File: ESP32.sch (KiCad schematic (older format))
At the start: 31 parts, among them J201 Conn_02x13_Odd_Even, J202 Conn_02x10_Odd_Even, J203 Conn_01x02, J204 Conn_01x06, J206 IO, J207 Conn_01x07, U201 ESP32-WROOM-32D

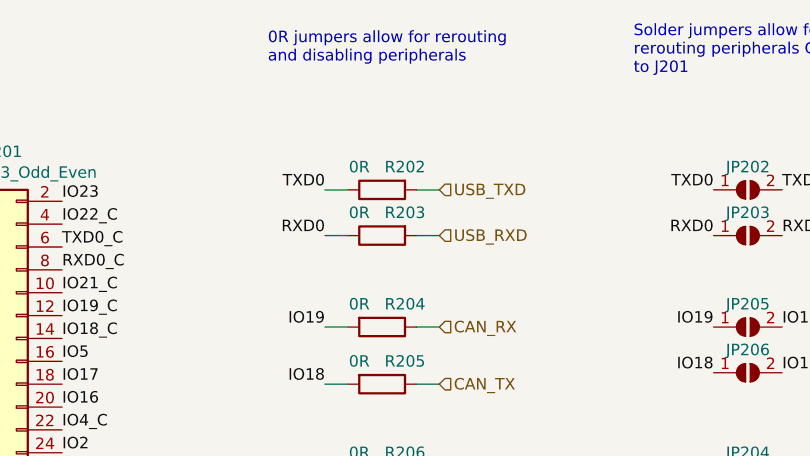
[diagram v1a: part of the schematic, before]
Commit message: - Swapped TXD0 & RXD0 between ESP32 and CH340C (U401) - (at the 0 Ohm Links) - U401 -> Pin 16 (VCC switched to 3V3) - U401 ->  Pin 4 (V3)  taken to 3V3
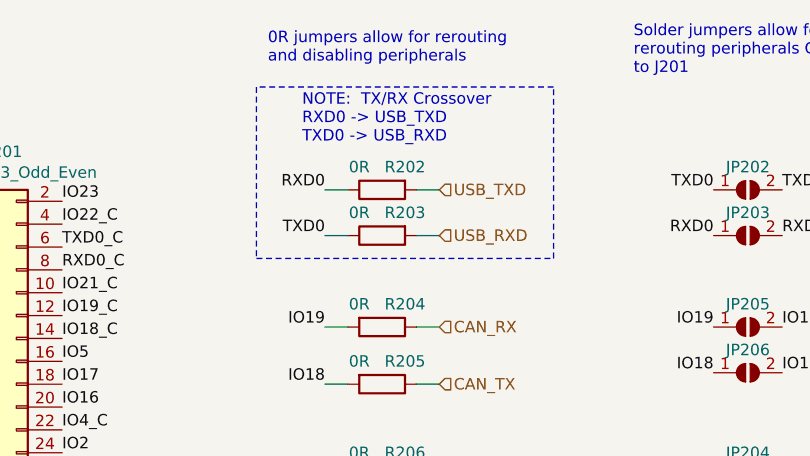
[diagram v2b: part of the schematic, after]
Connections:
- net RXD0: now also R202.1; no longer R203.1
- net TXD0: now also R203.1; no longer R202.1
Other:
- note added: "NOTE: TX/RX Crossover\nRXD0 -> USB_TXD \nTXD0 -> USB_RXD"
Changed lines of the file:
@@
 	0    -1   1    0
 $EndComp
+Text Label 7350 1650 2    50   ~ 0
+TXD0
 Text Label 7350 1450 2    50   ~ 0
-TXD0
-Text Label 7350 1650 2    50   ~ 0
 RXD0
 Wire Wire Line
@@
 Wire Wire Line
 	3750 7100 4150 7100
+Text Notes 7250 1250 0    50   ~ 0
+NOTE:  TX/RX Crossover\nRXD0 -> USB_TXD  \nTXD0 -> USB_RXD
+Wire Notes Line
+	7050 1750 8350 1750
+Wire Notes Line
+	8350 1750 8350 1000
+Wire Notes Line
+	8350 1000 7050 1000
+Wire Notes Line
+	7050 1000 7050 1750
 $EndSCHEMATC

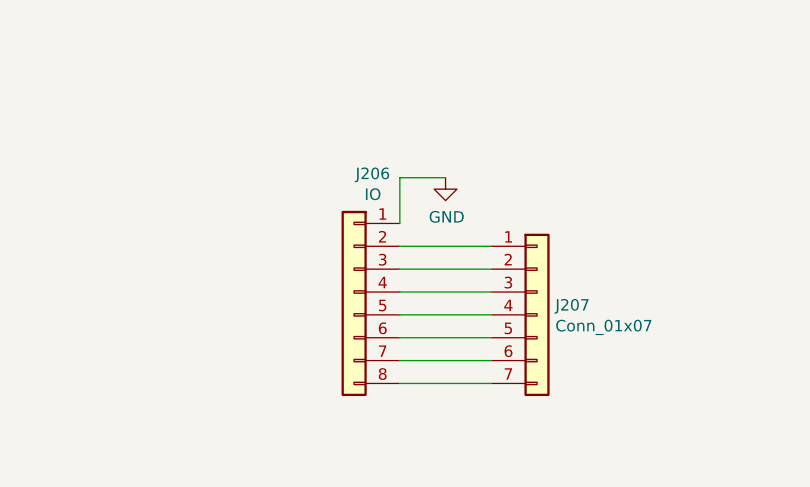
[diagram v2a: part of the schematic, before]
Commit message: Schematic of changes and  more Measurments on the Box / PCB Drawing
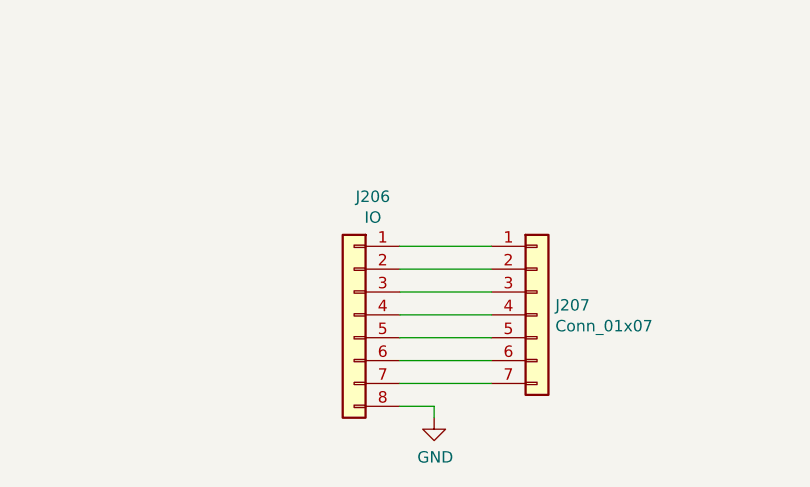
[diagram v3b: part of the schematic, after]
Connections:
- net GND: now also J206.8 (Pin_8); no longer J206.1 (Pin_1)
- net at J207.1 (Pin_1): now also J206.1 (Pin_1); no longer J206.2 (Pin_2)
- net at J207.2 (Pin_2): now also J206.2 (Pin_2); no longer J206.3 (Pin_3)
- net at J207.3 (Pin_3): now also J206.3 (Pin_3); no longer J206.4 (Pin_4)
- net at J207.4 (Pin_4): now also J206.4 (Pin_4); no longer J206.5 (Pin_5)
- net at J207.5 (Pin_5): now also J206.5 (Pin_5); no longer J206.6 (Pin_6)
- net at J207.6 (Pin_6): now also J206.6 (Pin_6); no longer J206.7 (Pin_7)
- net at J207.7 (Pin_7): now also J206.7 (Pin_7); no longer J206.8 (Pin_8)
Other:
- moved on the sheet: J206
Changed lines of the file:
@@
 L Connector_Generic:Conn_01x08 J206
 U 1 1 5FB25B29
-P 3550 6700
-F 0 "J206" H 3468 7217 50  0000 C CNN
-F 1 "IO" H 3468 7126 50  0000 C CNN
-F 2 "Connector_PinHeader_2.54mm:PinHeader_1x08_P2.54mm_Vertical" H 3550 6700 50  0001 C CNN
-F 3 "~" H 3550 6700 50  0001 C CNN
-	1    3550 6700
+P 3550 6800
+F 0 "J206" H 3468 7317 50  0000 C CNN
+F 1 "IO" H 3468 7226 50  0000 C CNN
+F 2 "Connector_PinHeader_2.54mm:PinHeader_1x08_P2.54mm_Vertical" H 3550 6800 50  0001 C CNN
+F 3 "~" H 3550 6800 50  0001 C CNN
+	1    3550 6800
 	-1   0    0    -1
 $EndComp
@@
 L power:GND #PWR0108
 U 1 1 5FB2B88B
-P 3950 6200
-F 0 "#PWR0108" H 3950 5950 50  0001 C CNN
-F 1 "GND" H 3955 6027 50  0000 C CNN
-F 2 "" H 3950 6200 50  0001 C CNN
-F 3 "" H 3950 6200 50  0001 C CNN
-	1    3950 6200
+P 3900 7250
+F 0 "#PWR0108" H 3900 7000 50  0001 C CNN
+F 1 "GND" H 3905 7077 50  0000 C CNN
+F 2 "" H 3900 7250 50  0001 C CNN
+F 3 "" H 3900 7250 50  0001 C CNN
+	1    3900 7250
 	1    0    0    -1
 $EndComp
-Wire Wire Line
-	3750 6400 3750 6200
-Wire Wire Line
-	3750 6200 3950 6200
 Wire Wire Line
 	3750 6500 4150 6500
@@
 Wire Notes Line
 	7050 1000 7050 1750
+Wire Wire Line
+	3750 7200 3900 7200
+Wire Wire Line
+	3900 7200 3900 7250
 $EndSCHEMATC

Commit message: Initial version with 40Pin header for Ethernet and re-route.
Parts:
- removed C201: 100nF, Capacitor_SMD:C_0402_1005Metric, symbol Device:C
- removed J204: Conn_01x06, Connector_PinHeader_2.54mm:PinHeader_1x06_P2.54mm_Vertical, symbol Connector_Generic:Conn_01x06
- removed R211: 1k, Resistor_SMD:R_0402_1005Metric, symbol Device:R
- removed R212: 10k, Resistor_SMD:R_0402_1005Metric, symbol Device:R
- added D1101, D1102: BAT54A, Package_TO_SOT_SMD:SOT-523, symbol Diode:BAT54A
- added R1103: 10k, Resistor_SMD:R_0402_1005Metric, symbol Device:R
- J201: value Conn_02x13_Odd_Even -> GPIO; footprint Connector_PinHeader_2.54mm:PinHeader_2x13_P2.54mm_Vertical -> Connector_PinHeader_2.54mm:PinHeader_2x20_P2.54mm_Vertical; symbol Connector_Generic:Conn_02x13_Odd_Even -> Connector_Generic:Conn_02x20_Odd_Even
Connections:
- net labels added: BOOT_AUTO, BOOT_KEY, IO16_C, IO2_C_SDA, IO32_C, IO33_C, IO34_C, IO35_C, IO4_C_SCL, RESET_AUTO, RESET_KEY
- net labels removed: BOOT, IO18_C, IO19_C, IO21_C, IO22_C, IO26_C, IO27_C, IO4_C, RESET
- wire segments 54 -> 81
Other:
- note added: "CAP here to slowdown \nreset on poweron"
- note added: "From Espressif Ethernet \nReference board\n"
- note added: "I2C/LCD"
- note added: "JTAG"
- note added: "RMII\nEthernet"
- note added: "Strap"
- note added: "UART0"
- moved on the sheet: C203, J202, J203, J206, J207, R201

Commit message: Add missed ESP32 Schematic to commit
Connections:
- wire segments 81 -> 97

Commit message: Pinout revamp after review and tidy up. - LED and DQ returned to current pins on Rev 0.1 - Freed JTAG pin from duplicate IO duty.
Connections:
- net labels added: IO16_C_SDA, IO17_C_SCL, IO4_C
- net labels removed: IO16_C, IO2_C_SDA, IO4_C_SCL
- wire segments 97 -> 82
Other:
- note added: "PHY_MDC\n"
- note added: "PHY_MDIO"
- note added: "PHY_RESET_N"
- note added: "RMII_EN"
- note added: "RMII_RXD0"
- note added: "RMII_RXD1"
- note added: "RMII_TXD0\n"
- note added: "RMII_TXD1\n"
- note added: "RMI_CRS_DV"
- moved on the sheet: C202, C203, J202, JP201, JP202, JP203, JP204, JP205, JP206, JP207, JP208, JP209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

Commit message: Updated Silkscreen for new GPIO pinout - Moved power header onto 0.1" grid with IO header. - Scattered GND vias.
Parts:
- C203: value 100nF -> 1uf; LCSC C1525 -> C52923
- J202: value Conn_02x10_Odd_Even -> Power; footprint Connector_PinHeader_2.54mm:PinHeader_2x04_P2.54mm_Vertical -> Connector_PinHeader_2.54mm:PinHeader_2x03_P2.54mm_Vertical; symbol Connector_Generic:Conn_02x04_Odd_Even -> Connector_Generic:Conn_02x03_Odd_Even
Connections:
- wire segments 82 -> 81
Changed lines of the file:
@@
 AR Path="/5FC3847D/5F9211FB" Ref="C203"  Part="1"
 F 0 "C203" H 2615 6946 50  0000 L CNN
-F 1 "100nF" H 2615 6855 50  0000 L CNN
+F 1 "1uf" H 2615 6855 50  0000 L CNN
 F 2 "Capacitor_SMD:C_0402_1005Metric" H 2538 6750 50  0001 C CNN
 F 3 "~" H 2500 6900 50  0001 C CNN
-F 4 "C1525" H 2500 6900 50  0001 C CNN "LCSC"
+F 4 "C52923" H 2500 6900 50  0001 C CNN "LCSC"
 	1    2500 6900
 	1    0    0    -1
@@
 Wire Wire Line
 	9650 5225 9650 5325
-Connection ~ 9650 5325
-Wire Wire Line
-	9650 5325 9650 5425
 $Comp
-L Connector_Generic:Conn_02x04_Odd_Even J202
+L Connector_Generic:Conn_02x03_Odd_Even J202
 U 1 1 5FA6B8ED
 P 9350 5225
 F 0 "J202" H 9200 5575 50  0000 C CNN
-F 1 "Conn_02x10_Odd_Even" H 9200 5475 50  0000 C CNN
-F 2 "Connector_PinHeader_2.54mm:PinHeader_2x04_P2.54mm_Vertical" H 9350 5225 50  0001 C CNN
+F 1 "Power" H 9200 5475 50  0000 C CNN
+F 2 "Connector_PinHeader_2.54mm:PinHeader_2x03_P2.54mm_Vertical" H 9350 5225 50  0001 C CNN
 F 3 "~" H 9350 5225 50  0001 C CNN
 F 4 "C358699" H 9350 5225 50  0001 C CNN "LCSC"

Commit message: Added a bunch of vias and tweaked the silkscreens
Also shoved some decoupling caps and vias a bit around to increase
ground fill areas.
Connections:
- wire segments 81 -> 80
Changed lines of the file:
@@
 	1    0    0    -1
 $EndComp
-Connection ~ 9150 5425
-Wire Wire Line
-	9150 5425 9150 5325
 Connection ~ 9150 5325
 Wire Wire Line
@@
 Solder jumpers allow for \nrerouting peripherals GPIOs\nto J201
 Wire Wire Line
-	9150 5425 9150 5825
-Wire Wire Line
 	9650 4875 9650 5125
 $Comp
@@
 L Connector_Generic:Conn_01x08 J206
 U 1 1 5FB25B29
-P 5150 6700
-F 0 "J206" H 5068 7217 50  0000 C CNN
-F 1 "IO" H 5068 7126 50  0000 C CNN
-F 2 "Connector_PinHeader_2.54mm:PinHeader_1x08_P2.54mm_Vertical" H 5150 6700 50  0001 C CNN
-F 3 "~" H 5150 6700 50  0001 C CNN
-	1    5150 6700
-	-1   0    0    -1
+P 5150 6800
+F 0 "J206" H 5068 7317 50  0000 C CNN
+F 1 "IO" H 5068 7226 50  0000 C CNN
+F 2 "Connector_PinHeader_2.54mm:PinHeader_1x08_P2.54mm_Vertical" H 5150 6800 50  0001 C CNN
+F 3 "~" H 5150 6800 50  0001 C CNN
+	1    5150 6800
+	-1   0    0    1
 $EndComp
 Wire Wire Line
@@
 Text Notes 4550 2100 0    50   ~ 0
 RMI_CRS_DV
+Wire Wire Line
+	9150 5325 9150 5825
 $EndSCHEMATC
